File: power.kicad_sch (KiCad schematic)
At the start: 60 parts, among them J17 CK-JS102011SAQN, J4 USB_C_Receptacle_USB2.0, Q1 SSM6J507NU, Q2 SSM6J507NU, Q3 SSM6J507NU, Q6 SSM6J507NU, U1 LM1117LDX, U2 LDFM33PVR, U5 MCP73213, U6 BQ29209, U7 STUSB4500QTR

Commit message: Annotate parts, add more buses
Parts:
- removed C14, C15, C16, C8: 1uF, Capacitor_SMD:C_0402_1005Metric, symbol Device:C_Small
- removed C17: 0.1uF, Capacitor_SMD:C_0402_1005Metric, symbol Device:C_Small
- removed C5: 4.7uF, Capacitor_SMD:C_0603_1608Metric, symbol Device:C_Small
- removed D24: ESDA25P35, footprints:1610, symbol synermycha-electronics:ESDA25P35
- removed D25: CDBQR0130L-HF, Diode_SMD:D_0402_1005Metric, symbol Device:D_Schottky_Small
- removed D28: ESDA25W, Package_TO_SOT_SMD:SOT-323_SC-70, symbol synermycha-electronics:ESDA25W
- removed J4: USB_C_Receptacle_USB2.0, Connector_USB:USB_C_Receptacle_GCT_USB4085, symbol synermycha-electronics-rescue:USB_C_Receptacle_USB2.0-Connector
- removed Q2: SSM6J507NU, footprints:UDFN6B, symbol synermycha-electronics:SSM6J507NU
- removed R16: 470, Resistor_SMD:R_0402_1005Metric, symbol Device:R_Small
- removed R17: 1K, Resistor_SMD:R_0402_1005Metric, symbol Device:R_Small
- removed R18, R28: 100K, Resistor_SMD:R_0402_1005Metric, symbol Device:R_Small
- removed R21: 18K, Resistor_SMD:R_0402_1005Metric, symbol Device:R_Small
- removed R47, R48: 22R, Resistor_SMD:R_0402_1005Metric, symbol Device:R_Small
- removed U7: STUSB4500QTR, Package_DFN_QFN:QFN-24-1EP_4x4mm_P0.5mm_EP2.7x2.7mm, symbol synermycha-electronics:STUSB4500QTR
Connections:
- net VDRIVE: no longer names the net of D29.1 (K1), D30.2 (A), Q6.3 (G), R34.1, U5.1 (VDD), U5.2 (VDD)
- no-connect marks 14 -> 5

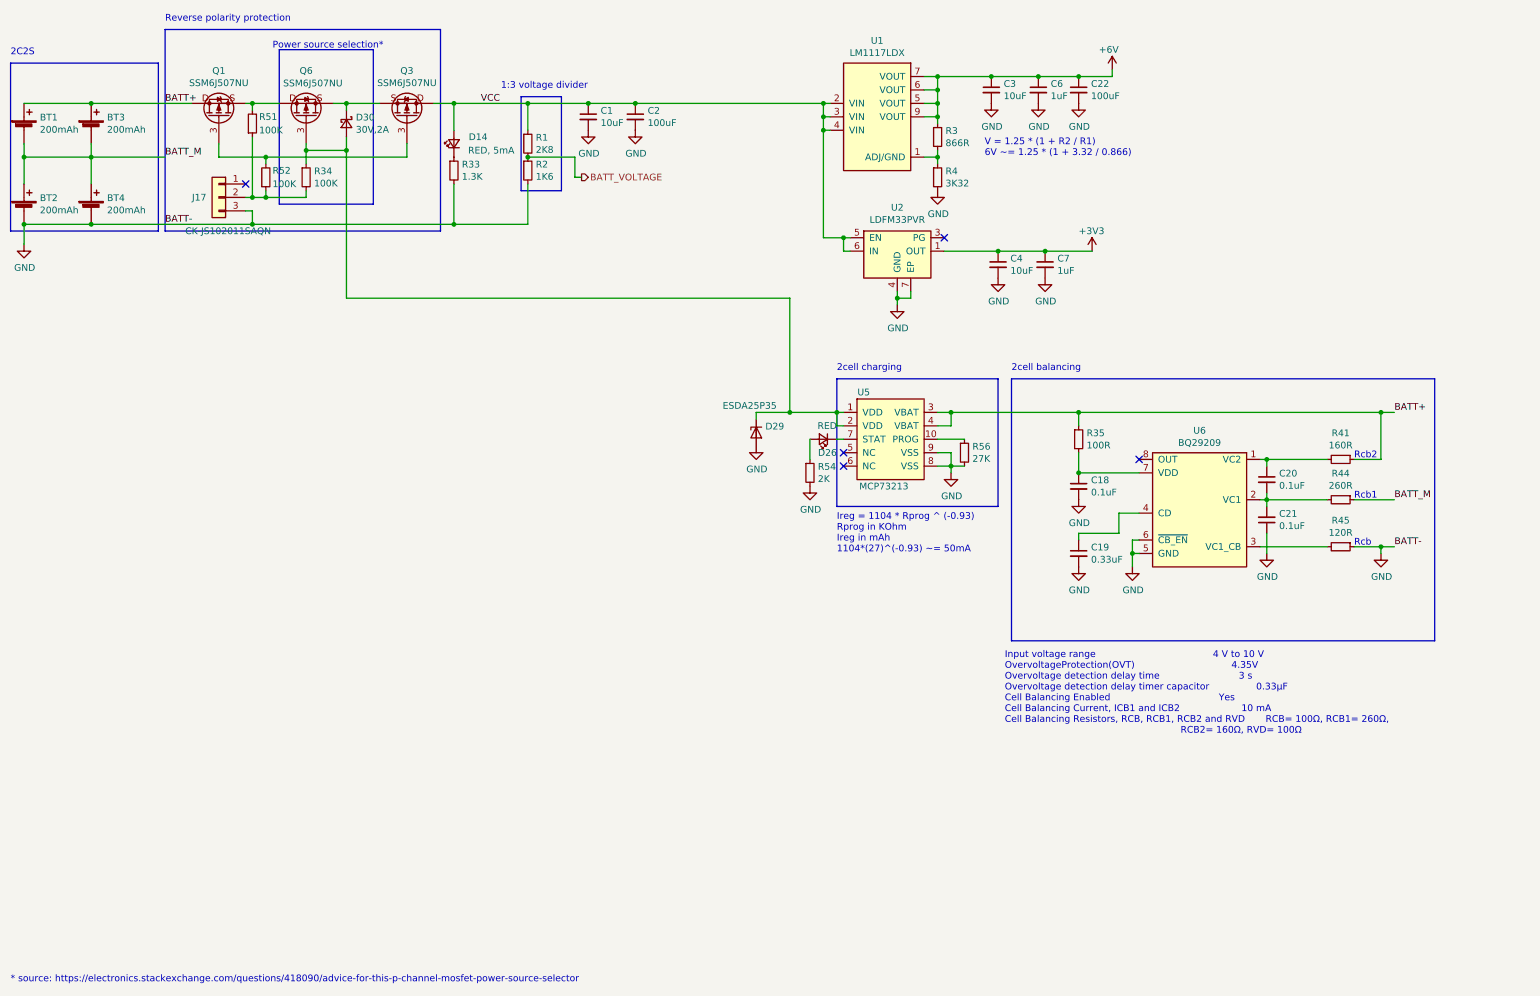
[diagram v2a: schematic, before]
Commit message: Cleanup power section, start over
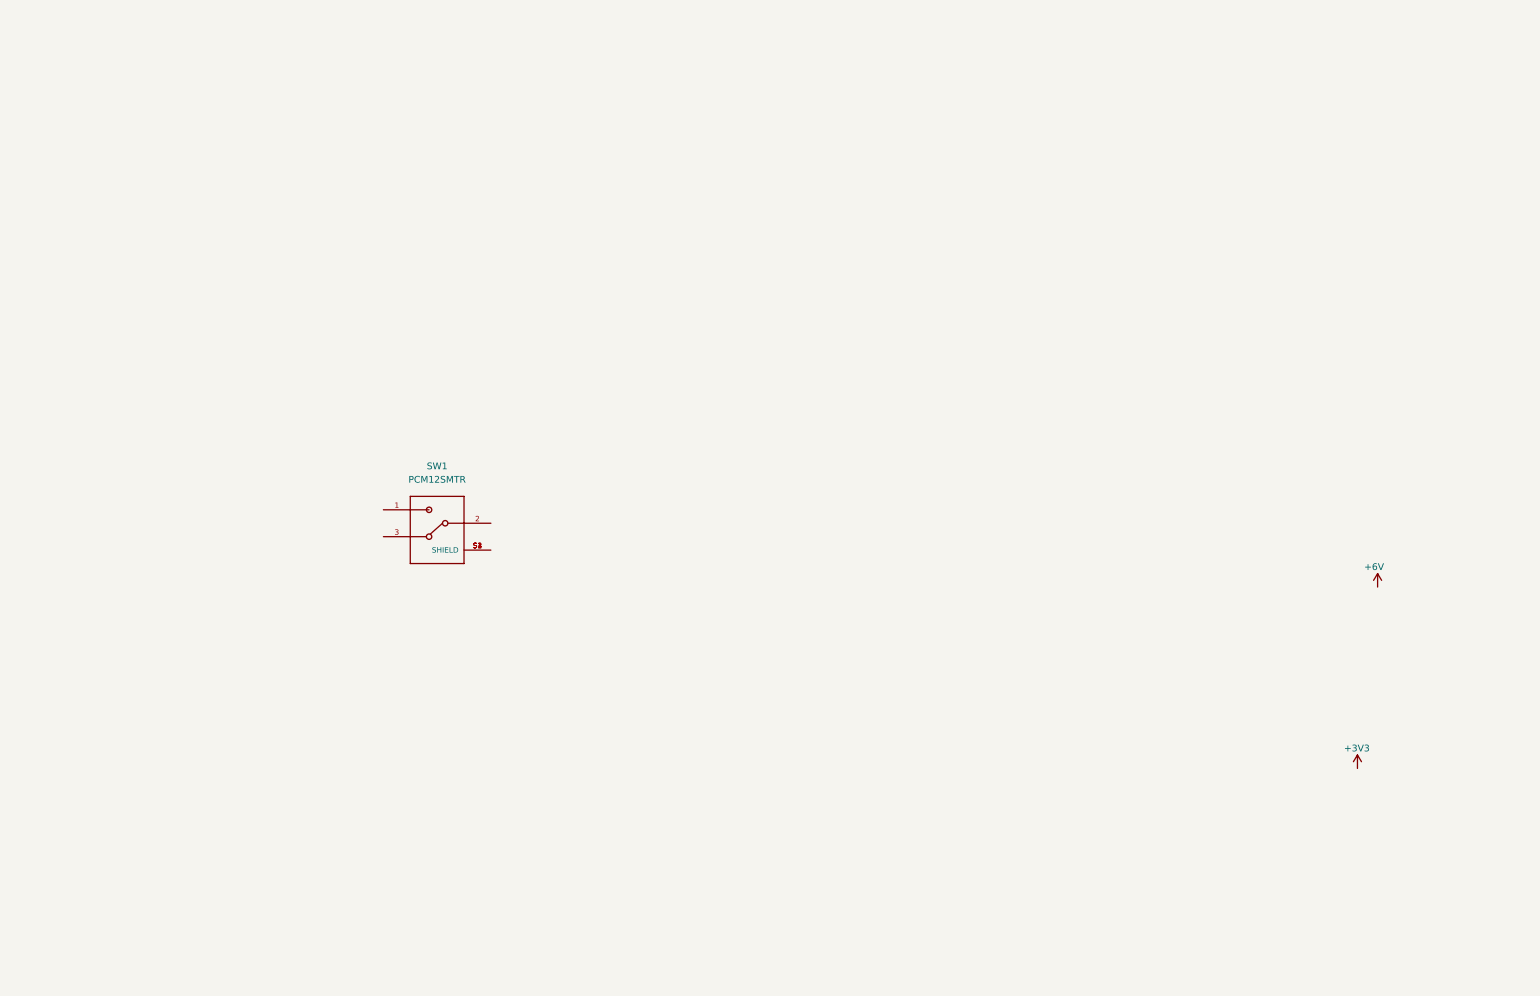
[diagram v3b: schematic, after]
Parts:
- removed BT1, BT2, BT3, BT4: 200mAh, Connector_PinHeader_1.27mm:PinHeader_1x02_P1.27mm_Vertical, symbol Device:Battery_Cell
- removed C1, C3, C4: 10uF, Capacitor_SMD:C_0603_1608Metric, symbol Device:C_Small
- removed C18, C20, C21: 0.1uF, Capacitor_SMD:C_0402_1005Metric, symbol Device:C_Small
- removed C19: 0.33uF, Capacitor_SMD:C_0402_1005Metric, symbol Device:C_Small
- removed C2, C22: 100uF, Capacitor_SMD:C_0805_2012Metric, symbol Device:C_Small
- removed C6, C7: 1uF, Capacitor_SMD:C_0402_1005Metric, symbol Device:C_Small
- removed D14: RED, 5mA, LED_SMD:LED_0402_1005Metric, symbol Device:LED_Small
- removed D26: RED, LED_SMD:LED_0402_1005Metric, symbol Device:LED_Small
- removed D29: ESDA25P35, footprints:1610, symbol synermycha-electronics:ESDA25P35
- removed D30: 30V,2A, Diode_SMD:D_SOD-123F, symbol Device:D_Schottky_Small
- removed J17: CK-JS102011SAQN, Button_Switch_SMD:SW_SPDT_CK-JS102011SAQN, symbol Connector_Generic:Conn_01x03
- removed Q1, Q3, Q6: SSM6J507NU, footprints:UDFN6B, symbol synermycha-electronics:SSM6J507NU
- removed R1: 2K8, Resistor_SMD:R_0402_1005Metric, symbol Device:R_Small
- removed R2: 1K6, Resistor_SMD:R_0402_1005Metric, symbol Device:R_Small
- removed R3: 866R, Resistor_SMD:R_0402_1005Metric, symbol Device:R_Small
- removed R33: 1.3K, Resistor_SMD:R_0402_1005Metric, symbol Device:R_Small
- removed R34, R51, R52: 100K, Resistor_SMD:R_0402_1005Metric, symbol Device:R_Small
- removed R35: 100R, Resistor_SMD:R_0402_1005Metric, symbol Device:R_Small
- removed R4: 3K32, Resistor_SMD:R_0402_1005Metric, symbol Device:R_Small
- removed R41: 160R, Resistor_SMD:R_0402_1005Metric, symbol Device:R_Small
- removed R44: 260R, Resistor_SMD:R_0402_1005Metric, symbol Device:R_Small
- removed R45: 120R, Resistor_SMD:R_0402_1005Metric, symbol Device:R_Small
- removed R54: 2K, Resistor_SMD:R_0402_1005Metric, symbol Device:R_Small
- removed R56: 27K, Resistor_SMD:R_0402_1005Metric, symbol Device:R_Small
- removed U1: LM1117LDX, Package_SON:WSON-8_4x4mm_P0.8mm, symbol LM1117:LM1117LDX
- removed U2: LDFM33PVR, Package_DFN_QFN:DFN-6-1EP_2x2mm_P0.5mm_EP0.61x1.42mm, symbol synermycha-electronics:LDFM33PVR
- removed U5: MCP73213, Package_DFN_QFN:DFN-10-1EP_3x3mm_P0.5mm_EP1.55x2.48mm, symbol synermycha-electronics:MCP73213
- removed U6: BQ29209, Package_SON:HVSON-8-1EP_3x3mm_P0.65mm_EP1.6x2.4mm, symbol synermycha-electronics:BQ29209
- added SW1: PCM12SMTR, antmicro-footprints:PCM12SMTR, symbol antmicroSlideSwitches:PCM12SMTR
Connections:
- new net: SW1.S1 (SHIELD), SW1.S2 (SHIELD), SW1.S3 (SHIELD), SW1.S4 (SHIELD)
- no-connect marks 5 -> 0
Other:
- note removed: "* source: https://electronics.stackexchange.com/questions/418090/advice-for-this-p-channel-mosfet-power-source-selector"
- note removed: "1:3 voltage divider"
- note removed: "2C2S"
- note removed: "2cell balancing"
- note removed: "2cell charging"
- note removed: "Input voltage range 4 V to 10 V OvervoltageProtection(OVT) 4.35V Overvoltage detection delay time 3 s Overvoltage detection delay timer capacitor 0.33μF Cell Balancing Enabled Yes Cell Balancing Current, ICB1 and ICB2 10 mA Cell Balancing Resistors, RCB, RCB1, RCB2 and RVD RCB= 100Ω, RCB1= 260Ω, RCB2= 160Ω, RVD= 100Ω"
- note removed: "Ireg = 1104 * Rprog ^ (-0.93) Rprog in KOhm Ireg in mAh 1104*(27)^(-0.93) ~= 50mA"
- note removed: "Power source selection*"
- note removed: "Rcb"
- note removed: "Rcb1"
- note removed: "Rcb2"
- note removed: "Reverse polarity protection"
- note removed: "V = 1.25 * (1 + R2 / R1) 6V ~= 1.25 * (1 + 3.32 / 0.866)"

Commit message: Start power section from scratch
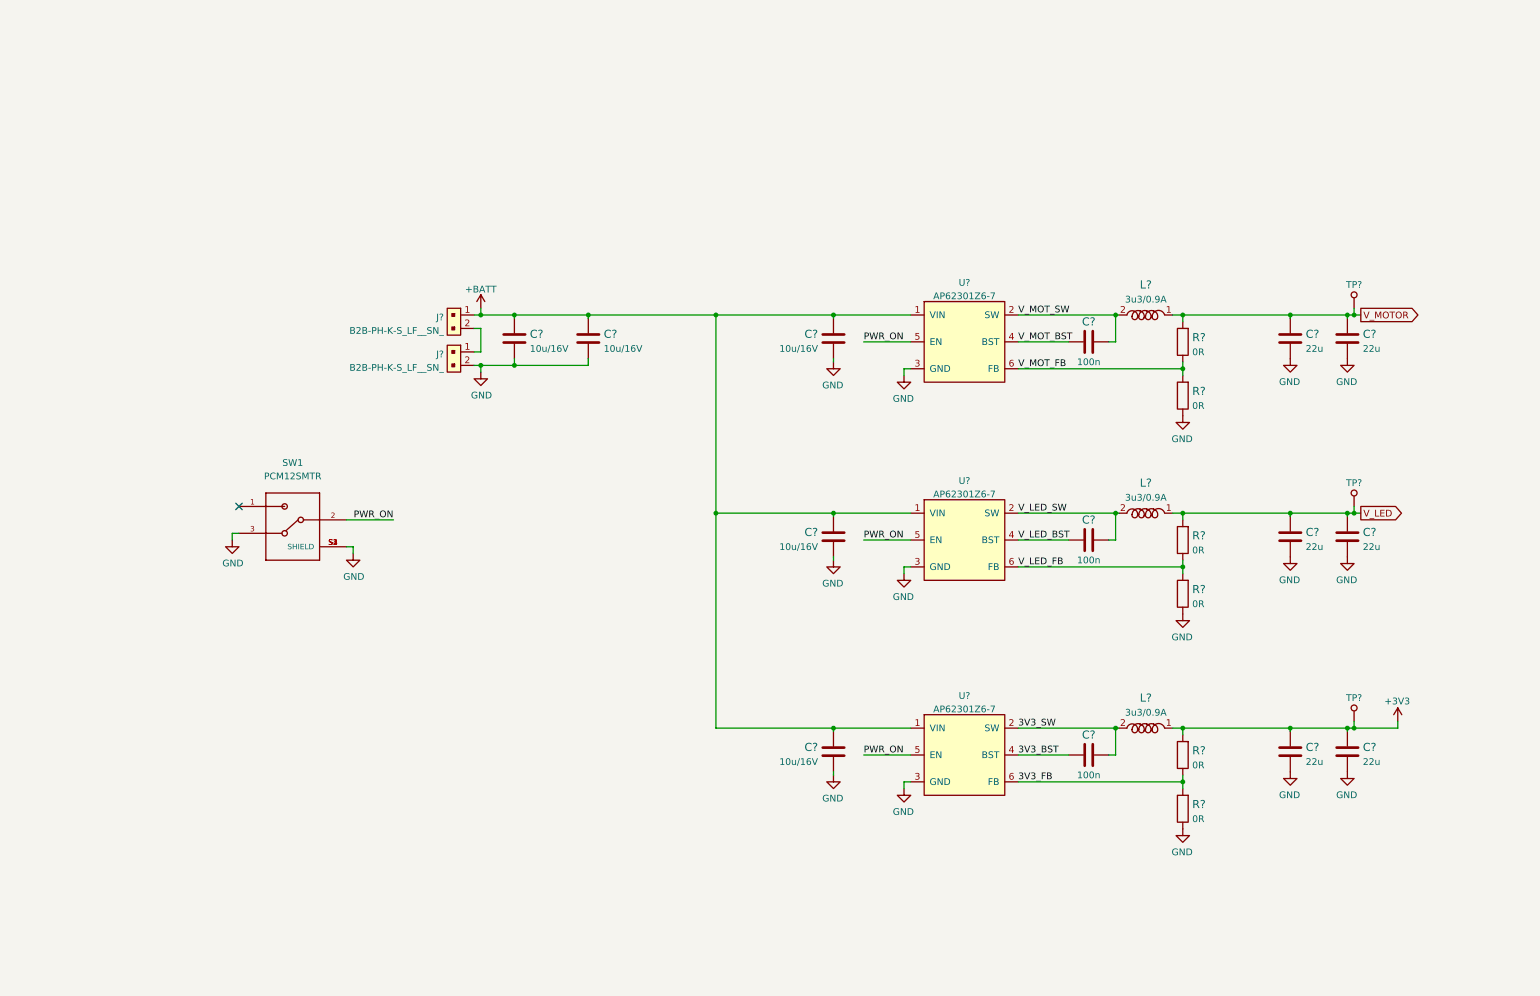
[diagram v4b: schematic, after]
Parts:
- added C? (x6): C_22u_0805_10V, antmicro-footprints:0805-cap, symbol antmicroCapacitorsmisc:C_22u_0805_10V
- added C? (x3): C_100n_0402, antmicro-footprints:0402-cap, symbol antmicroCapacitors0402:C_100n_0402
- added C? (x5): C_10u_16V_0603, antmicro-footprints:0603-cap, symbol antmicroCapacitors0603:C_10u_16V_0603
- added J? (x2): B2B-PH-K-S_LF__SN_, antmicro-footprints:PinHeader_1x2_P2mm_Drill1mm, symbol antmicroRectangularConnectorsHeadersMalePins:B2B-PH-K-S_LF__SN_
- added L? (x3): MLP2012S3R3MT, antmicro-footprints:0805-res, symbol antmicroFixedInductors:MLP2012S3R3MT
- added R? (x6): R_0R_0402, antmicro-footprints:0402-res, symbol antmicroResistors0402:R_0R_0402
- added TP? (x3): TP_SMD_0_75MM, antmicro-footprints:Testpoint_smd_0_75mm, symbol antmicroTestPoints:TP_SMD_0_75MM
- added U? (x3): AP62301Z6-7, antmicro-footprints:SOT-563, symbol antmicroDCDCConverters:AP62301Z6-7
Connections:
- net +3V3: now also C?.1, C?.1, L?.1, R?.2, TP?.1
- net PWR_ON: now reaches SW1.2
- net PWR_ON: now also U?.5 (EN), U?.5 (EN), U?.5 (EN)
- net GND: now reaches SW1.3
- net GND: now also SW1.S1 (SHIELD), SW1.S2 (SHIELD), SW1.S3 (SHIELD), SW1.S4 (SHIELD), C?.2, C?.2, C?.2, C?.2, C?.2, C?.2, C?.2, C?.2, C?.2, C?.2, C?.2, J?.2, R?.1, R?.1, R?.1, U?.3 (GND), U?.3 (GND), U?.3 (GND)
- new net: J?.1, J?.2
- new net +BATT: C?.1, C?.1, C?.1, C?.1, C?.1, J?.1, U?.1 (VIN), U?.1 (VIN), U?.1 (VIN)
- new net 3V3_BST: C?.1, U?.4 (BST)
- new net 3V3_FB: R?.1, R?.2, U?.6 (FB)
- new net 3V3_SW: C?.2, L?.2, U?.2 (SW)
- new net V_LED: C?.1, C?.1, L?.1, R?.2, TP?.1
- new net V_LED_BST: C?.1, U?.4 (BST)
- new net V_LED_FB: R?.1, R?.2, U?.6 (FB)
- new net V_LED_SW: C?.2, L?.2, U?.2 (SW)
- new net V_MOTOR: C?.1, C?.1, L?.1, R?.2, TP?.1
- new net V_MOT_BST: C?.1, U?.4 (BST)
- new net V_MOT_FB: R?.1, R?.2, U?.6 (FB)
- new net V_MOT_SW: C?.2, L?.2, U?.2 (SW)
- no-connect marks 0 -> 1
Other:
- moved on the sheet: SW1
